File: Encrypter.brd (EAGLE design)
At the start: 60.3 x 73 mm, 5 parts, among them IC1 PIC16LF1517/19P

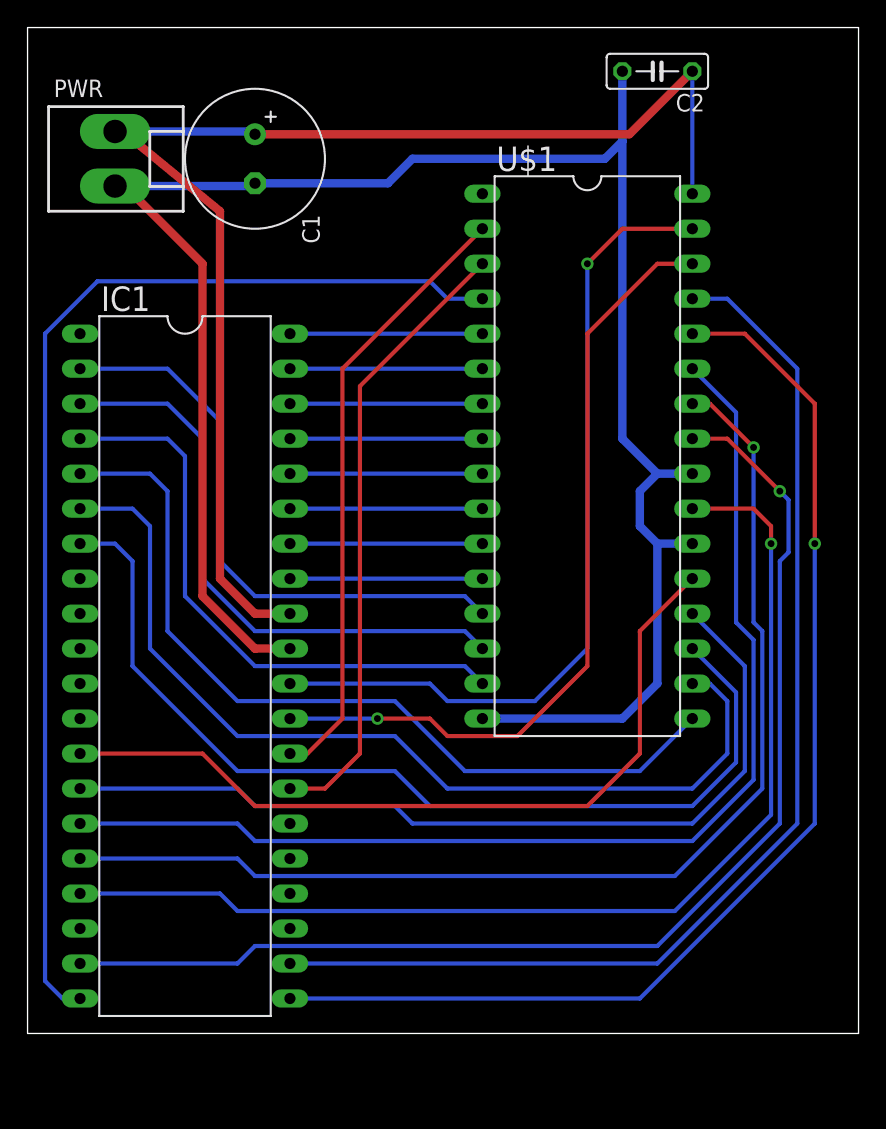
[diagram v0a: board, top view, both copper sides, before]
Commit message: Encrypter work
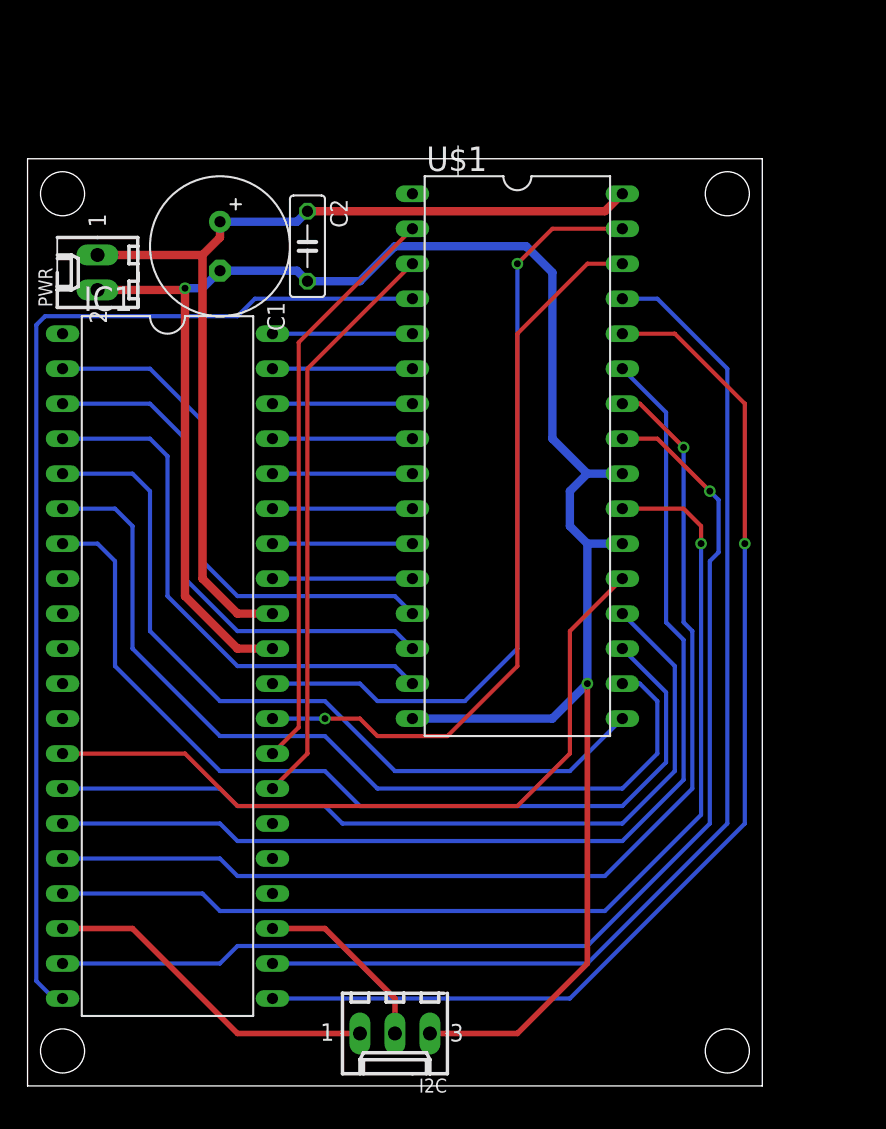
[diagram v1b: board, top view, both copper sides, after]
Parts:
- added I2C: 22-27-2031-03, con-molex:6410-03
- PWR: value (none) -> 22-27-2021-02; device con-molex:KK-156-2 -> con-molex:6410-02
- moved C2 28.4 mm to (20.3, 57.1), turned to 270 degrees
- moved PWR 8.35 mm to (5.08, 55.2), turned to 90 degrees
- moved C1 6.84 mm to (14.0, 57.1)
- moved U$1 5.08 mm to (35.6, 41.9)
- moved IC1 1.27 mm to (10.2, 26.7)
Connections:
- new net N$1: I2C.1, IC1.18
- new net N$2: I2C.2, IC1.23
- net GND: now also I2C.3
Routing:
- net +5V: track 95.3 -> 70.2 mm
- net N$1: track 0.00 -> 24.7 mm
- net N$2: track 0.00 -> 13.5 mm
- net GND: track 144.3 -> 150.6 mm, vias 0 -> 2
- net A12: track 83.9 -> 78.2 mm
- net O7: track 58.1 -> 54.3 mm
- net O5: track 70.9 -> 67.1 mm
- net O4: track 68.5 -> 64.7 mm
- net O3: track 60.9 -> 57.1 mm
- net A9: track 83.5 -> 79.7 mm
- net A7: track 14.0 -> 10.2 mm
- net A6: track 14.0 -> 10.2 mm
- net A5: track 14.0 -> 10.2 mm
- net A4: track 14.0 -> 10.2 mm
- net A3: track 14.0 -> 10.2 mm
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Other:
- board size 60.3 x 73 mm -> 53.3 x 67.3 mm
